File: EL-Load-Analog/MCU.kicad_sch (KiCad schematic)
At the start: 2 parts, among them J4 Conn_02x08_Odd_Even, J8 Conn_02x08_Odd_Even

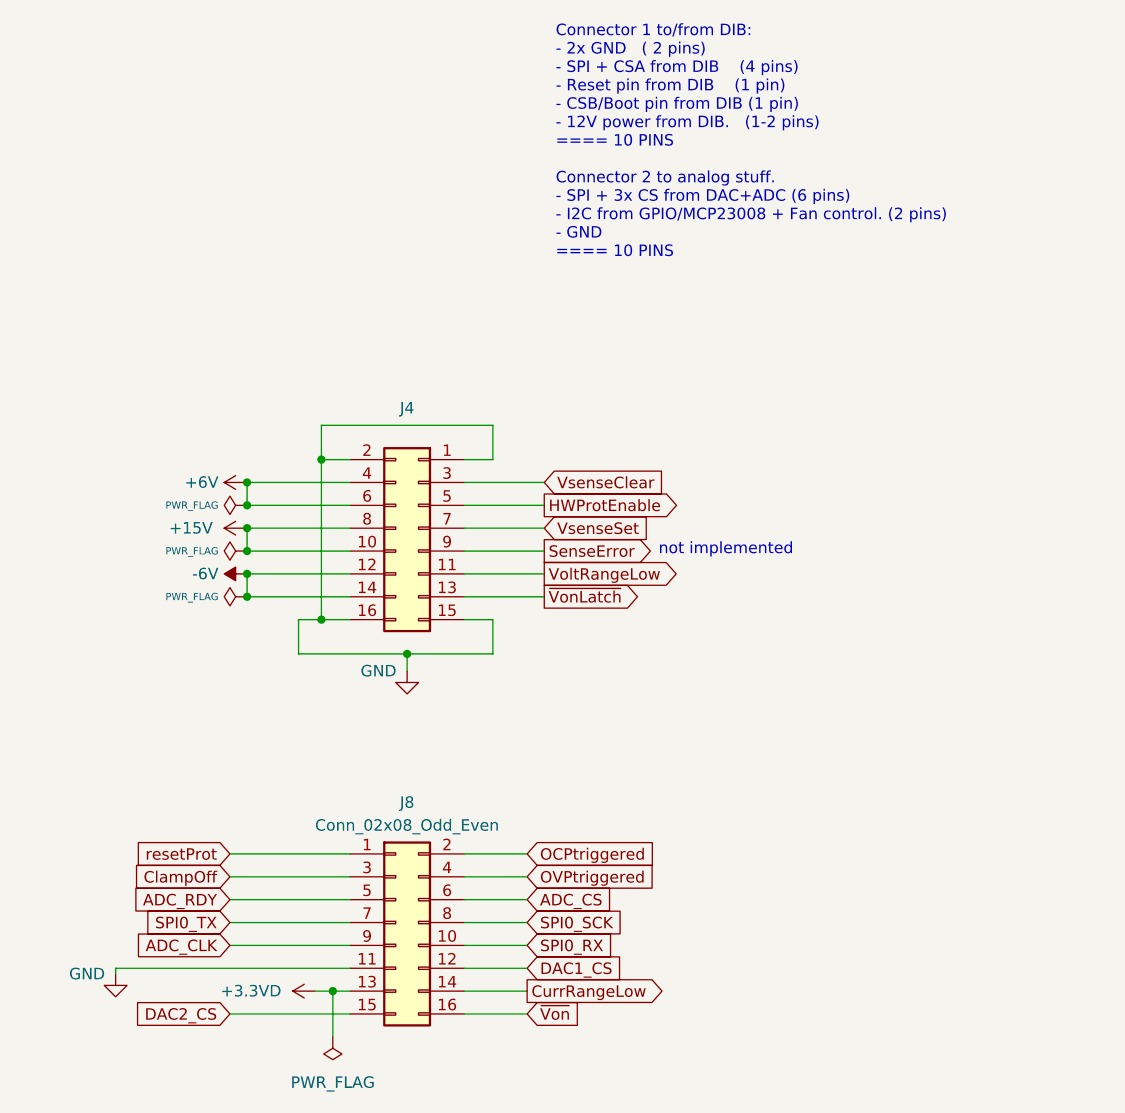
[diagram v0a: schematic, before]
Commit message: Added heatsink moutingholes, reverse polarity, moved snubbers.
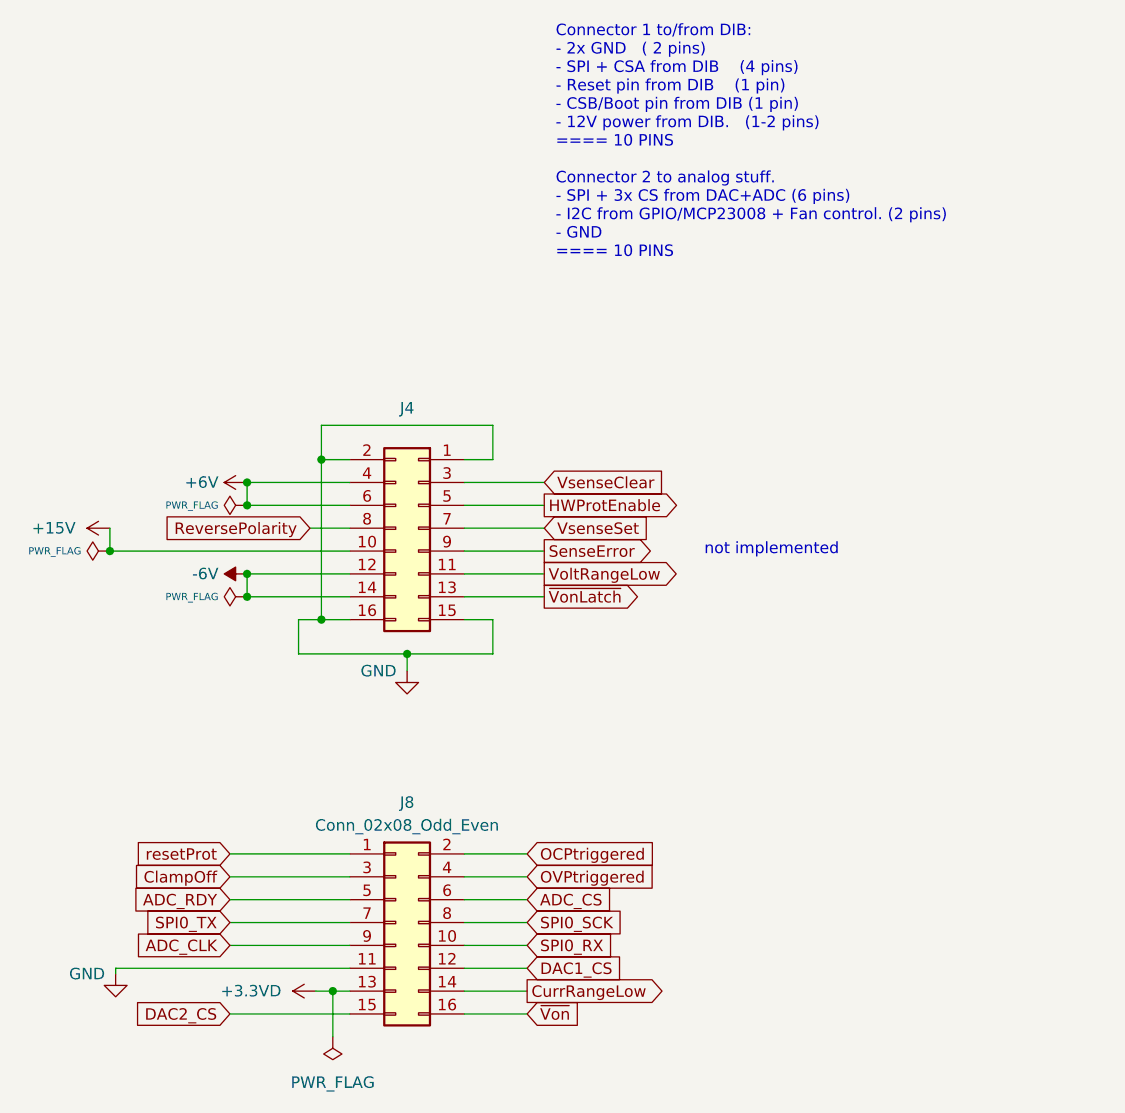
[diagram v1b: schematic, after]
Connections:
- net +15V: no longer J4.8 (Pin_8)
- new net ReversePolarity: J4.8 (Pin_8)
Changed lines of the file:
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@@
     (comment 1 "License: CERN-OHL-W-2.0")
   )
-  (junction (at 61.595 74.295) (diameter 0) (color 0 0 0 0)
-  )
-  (junction (at 61.595 71.755) (diameter 0) (color 0 0 0 0)
+  (junction (at 46.355 74.295) (diameter 0) (color 0 0 0 0)
   )
   (junction (at 69.85 81.915) (diameter 0) (color 0 0 0 0)
@@
     (stroke (width 0) (type default))
   )
-  (wire (pts (xy 61.595 71.755) (xy 61.595 74.295))
+  (wire (pts (xy 46.355 71.755) (xy 46.355 74.295))
     (stroke (width 0) (type default))
   )
@@
     (stroke (width 0) (type default))
   )
+  (wire (pts (xy 68.58 71.755) (xy 73.025 71.755))
+    (stroke (width 0) (type default))
+  )
   (wire (pts (xy 85.725 81.915) (xy 88.9 81.915))
     (stroke (width 0) (type default))
@@
     (stroke (width 0) (type default))
   )
-  (wire (pts (xy 61.595 74.295) (xy 73.025 74.295))
+  (wire (pts (xy 46.355 74.295) (xy 73.025 74.295))
     (stroke (width 0) (type default))
   )
@@
   )
   (wire (pts (xy 59.69 110.49) (xy 73.025 110.49))
-    (stroke (width 0) (type default))
-  )
-  (wire (pts (xy 61.595 71.755) (xy 73.025 71.755))
     (stroke (width 0) (type default))
   )
@@
     (effects (font (size 1.27 1.27)) (justify left bottom))
   )
-  (text "not implemented" (at 107.315 74.93 0)
+  (text "not implemented" (at 112.395 74.93 0)
     (effects (font (size 1.27 1.27)) (justify left bottom))
   )
@@
     (effects (font (size 1.27 1.27)) (justify left))
     (property "Intersheetrefs" "${INTERSHEET_REFS}" (at 99.0024 125.73 0)
-      (effects (font (size 1.27 1.27)) (justify left) hide)
+      (effects (font (size 1.27 1.27)) (justify left))
     )
   )
@@
     (effects (font (size 1.27 1.27)) (justify left))
     (property "Intersheetrefs" "${INTERSHEET_REFS}" (at 107.832 110.49 0)
-      (effects (font (size 1.27 1.27)) (justify left) hide)
+      (effects (font (size 1.27 1.27)) (justify left))
     )
   )
@@
     (effects (font (size 1.27 1.27)) (justify left))
     (property "Intersheetrefs" "${INTERSHEET_REFS}" (at 108.9204 123.19 0)
-      (effects (font (size 1.27 1.27)) (justify left) hide)
+      (effects (font (size 1.27 1.27)) (justify left))
     )
   )
@@
     (effects (font (size 1.27 1.27)) (justify left))
     (property "Intersheetrefs" "${INTERSHEET_REFS}" (at 103.901 120.65 0)
-      (effects (font (size 1.27 1.27)) (justify left) hide)
+      (effects (font (size 1.27 1.27)) (justify left))
     )
   )
@@
     (effects (font (size 1.27 1.27)) (justify left))
     (property "Intersheetrefs" "${INTERSHEET_REFS}" (at 102.1988 112.9506 0)
-      (effects (font (size 1.27 1.27)) (justify left) hide)
+      (effects (font (size 1.27 1.27)) (justify left))
     )
   )
@@
     (effects (font (size 1.27 1.27)) (justify left))
     (property "Intersheetrefs" "${INTERSHEET_REFS}" (at 107.095 71.755 0)
-      (effects (font (size 1.27 1.27)) (justify left) hide)
+      (effects (font (size 1.27 1.27)) (justify left))
     )
   )
@@
     (effects (font (size 1.27 1.27)) (justify left))
     (property "Intersheetrefs" "${INTERSHEET_REFS}" (at 106.0478 79.375 0)
-      (effects (font (size 1.27 1.27)) (justify left) hide)
+      (effects (font (size 1.27 1.27)) (justify left))
     )
   )
@@
     (effects (font (size 1.27 1.27)) (justify left))
     (property "Intersheetrefs" "${INTERSHEET_REFS}" (at 104.1341 115.4906 0)
-      (effects (font (size 1.27 1.27)) (justify left) hide)
+      (effects (font (size 1.27 1.27)) (justify left))
     )
   )
@@
     (effects (font (size 1.27 1.27)) (justify right))
     (property "Intersheetrefs" "${INTERSHEET_REFS}" (at 49.3457 115.57 0)
-      (effects (font (size 1.27 1.27)) (justify right) hide)
+      (effects (font (size 1.27 1.27)) (justify right))
     )
   )
@@
     (effects (font (size 1.27 1.27)) (justify left))
     (property "Intersheetrefs" "${INTERSHEET_REFS}" (at 108.0134 107.95 0)
-      (effects (font (size 1.27 1.27)) (justify left) hide)
+      (effects (font (size 1.27 1.27)) (justify left))
     )
   )
@@
     (effects (font (size 1.27 1.27)) (justify right))
     (property "Intersheetrefs" "${INTERSHEET_REFS}" (at 48.5594 113.03 0)
-      (effects (font (size 1.27 1.27)) (justify right) hide)
+      (effects (font (size 1.27 1.27)) (justify right))
     )
   )
@@
     (effects (font (size 1.27 1.27)) (justify left))
     (property "Intersheetrefs" "${INTERSHEET_REFS}" (at 107.7412 74.295 0)
-      (effects (font (size 1.27 1.27)) (justify left) hide)
+      (effects (font (size 1.27 1.27)) (justify left))
     )
   )
@@
     (effects (font (size 1.27 1.27)) (justify left))
     (property "Intersheetrefs" "${INTERSHEET_REFS}" (at 110.5834 69.215 0)
-      (effects (font (size 1.27 1.27)) (justify left) hide)
+      (effects (font (size 1.27 1.27)) (justify left))
     )
   )
@@
     (effects (font (size 1.27 1.27)) (justify right))
     (property "Intersheetrefs" "${INTERSHEET_REFS}" (at 48.1361 107.95 0)
-      (effects (font (size 1.27 1.27)) (justify right) hide)
+      (effects (font (size 1.27 1.27)) (justify right))
     )
   )
@@
     (effects (font (size 1.27 1.27)) (justify right))
     (property "Intersheetrefs" "${INTERSHEET_REFS}" (at 48.0758 110.49 0)
-      (effects (font (size 1.27 1.27)) (justify right) hide)
+      (effects (font (size 1.27 1.27)) (justify right))
     )
   )
@@
     (effects (font (size 1.27 1.27)) (justify left))
     (property "Intersheetrefs" "${INTERSHEET_REFS}" (at 109.0302 66.675 0)
-      (effects (font (size 1.27 1.27)) (justify left) hide)
+      (effects (font (size 1.27 1.27)) (justify left))
+    )
+  )
+  (global_label "ReversePolarity" (shape input) (at 68.58 71.755 180) (fields_autoplaced)
+    (effects (font (size 1.27 1.27)) (justify right))
+    (property "Intersheetrefs" "${INTERSHEET_REFS}" (at 50.9596 71.755 0)
+      (effects (font (size 1.27 1.27)) (justify right))
     )
   )
@@
     (effects (font (size 1.27 1.27)) (justify right))
     (property "Intersheetrefs" "${INTERSHEET_REFS}" (at 48.6199 118.11 0)
-      (effects (font (size 1.27 1.27)) (justify right) hide)
+      (effects (font (size 1.27 1.27)) (justify right))
     )
   )
@@
     (effects (font (size 1.27 1.27)) (justify left))
     (property "Intersheetrefs" "${INTERSHEET_REFS}" (at 110.4625 76.835 0)
-      (effects (font (size 1.27 1.27)) (justify left) hide)
+      (effects (font (size 1.27 1.27)) (justify left))
     )
   )
@@
     (effects (font (size 1.27 1.27)) (justify left))
     (property "Intersheetrefs" "${INTERSHEET_REFS}" (at 102.8641 118.0306 0)
-      (effects (font (size 1.27 1.27)) (justify left) hide)
+      (effects (font (size 1.27 1.27)) (justify left))
     )
   )
@@
     (effects (font (size 1.27 1.27)) (justify right))
     (property "Intersheetrefs" "${INTERSHEET_REFS}" (at 48.9917 125.6506 0)
-      (effects (font (size 1.27 1.27)) (justify right) hide)
+      (effects (font (size 1.27 1.27)) (justify right))
     )
   )
@@
     )
   )
-  (symbol (lib_id "power:+15V") (at 61.595 71.755 90) (unit 1)
-    (in_bom yes) (on_board yes) (dnp no) (fields_autoplaced)
-    (property "Reference" "#PWR0175" (at 65.405 71.755 0)
-      (effects (font (size 1.27 1.27)) hide)
-    )
-    (property "Value" "+15V" (at 57.785 71.755 90)
-      (effects (font (size 1.27 1.27)) (justify left))
-    )
-    (property "Footprint" "" (at 61.595 71.755 0)
-      (effects (font (size 1.27 1.27)) hide)
-    )
-    (property "Datasheet" "" (at 61.595 71.755 0)
+  (symbol (lib_id "power:+15V") (at 46.355 71.755 90) (unit 1)
+    (in_bom yes) (on_board yes) (dnp no) (fields_autoplaced)
+    (property "Reference" "#PWR0175" (at 50.165 71.755 0)
+      (effects (font (size 1.27 1.27)) hide)
+    )
+    (property "Value" "+15V" (at 42.545 71.755 90)
+      (effects (font (size 1.27 1.27)) (justify left))
+    )
+    (property "Footprint" "" (at 46.355 71.755 0)
+      (effects (font (size 1.27 1.27)) hide)
+    )
+    (property "Datasheet" "" (at 46.355 71.755 0)
       (effects (font (size 1.27 1.27)) hide)
     )
@@
     )
   )
-  (symbol (lib_id "power:PWR_FLAG") (at 61.595 74.295 90) (unit 1)
-    (in_bom yes) (on_board yes) (dnp no) (fields_autoplaced)
-    (property "Reference" "#FLG03" (at 59.69 74.295 0)
-      (effects (font (size 1.27 1.27)) hide)
-    )
-    (property "Value" "PWR_FLAG" (at 58.42 74.295 90)
+  (symbol (lib_id "power:PWR_FLAG") (at 46.355 74.295 90) (unit 1)
+    (in_bom yes) (on_board yes) (dnp no) (fields_autoplaced)
+    (property "Reference" "#FLG03" (at 44.45 74.295 0)
+      (effects (font (size 1.27 1.27)) hide)
+    )
+    (property "Value" "PWR_FLAG" (at 43.18 74.295 90)
       (effects (font (size 0.8 0.8)) (justify left))
     )
-    (property "Footprint" "" (at 61.595 74.295 0)
-      (effects (font (size 1.27 1.27)) hide)
-    )
-    (property "Datasheet" "~" (at 61.595 74.295 0)
-      (effects (font (size 1.27 1.27)) hide)
-    )
+    (property "Footprint" "" (at 46.355 74.295 0)
+      (effects (font (size 1.27 1.27)) hide)
+    )
+    (property "Datasheet" "~" (at 46.355 74.295 0)
+      (effects (font (size 1.27 1.27)) hide)
+    )

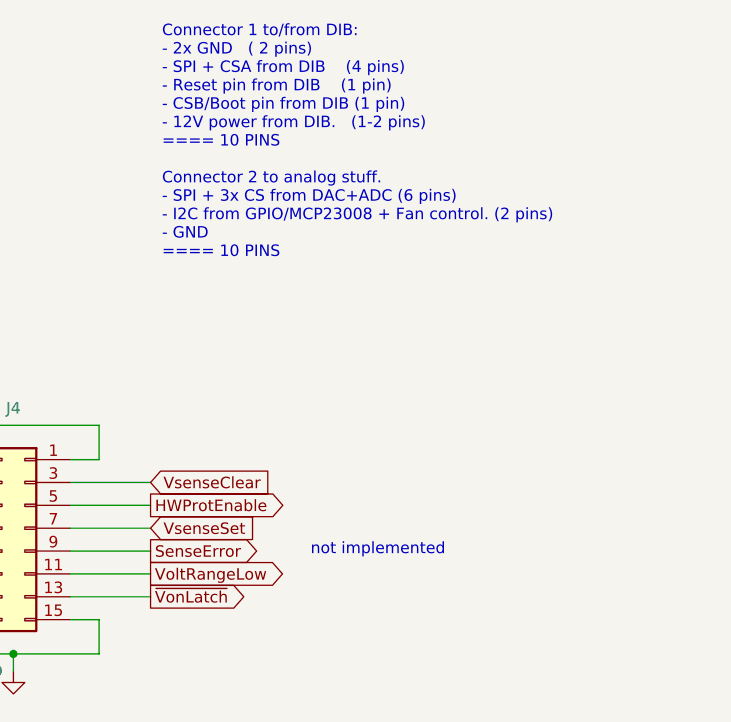
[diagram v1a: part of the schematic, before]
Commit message: v4 Analog board design. Features reverse polarity, remote sense error and new clamping circuitry.
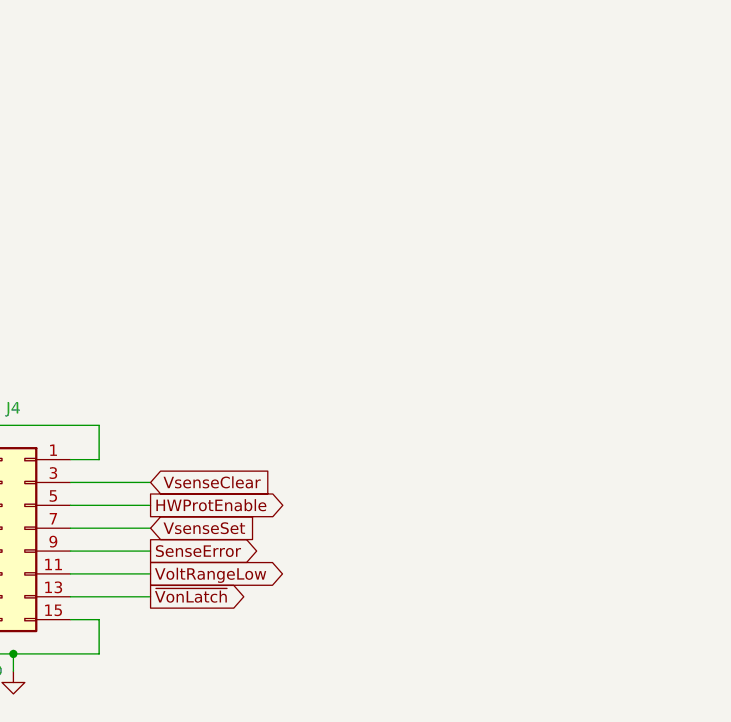
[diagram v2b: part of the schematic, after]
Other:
- note removed: "Connector 1 to/from DIB: - 2x GND ( 2 pins) - SPI + CSA from DIB (4 pins) - Reset pin from DIB (1 pin) - CSB/Boot pin from DIB (1 pin) - 12V power from DIB. (1-2 pins) ==== 10 PINS Connector 2 to analog stuff. - SPI + 3x CS from DAC+ADC (6 pins) - I2C from GPIO/MCP23008 + Fan control. (2 pins) - GND ==== 10 PINS"
- note removed: "not implemented"
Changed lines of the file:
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@@
   (title_block
     (title "Electronic Load Analog Test Board")
-    (date "2024-02-06")
+    (date "2024-11-10")
     (rev "${VERSION}")
     (comment 1 "License: CERN-OHL-W-2.0")
@@
     (stroke (width 0) (type default))
   )
-  (text "Connector 1 to/from DIB:\n- 2x GND   ( 2 pins)\n- SPI + CSA from DIB    (4 pins)\n- Reset pin from DIB    (1 pin)\n- CSB/Boot pin from DIB (1 pin)\n- 12V power from DIB.   (1-2 pins)\n==== 10 PINS\n\nConnector 2 to analog stuff.\n- SPI + 3x CS from DAC+ADC (6 pins)\n- I2C from GPIO/MCP23008 + Fan control. (2 pins)\n- GND\n==== 10 PINS\n"
-    (at 95.885 41.91 0)
-    (effects (font (size 1.27 1.27)) (justify left bottom))
-  )
-  (text "not implemented" (at 112.395 74.93 0)
-    (effects (font (size 1.27 1.27)) (justify left bottom))
-  )
   (global_label "~{Von}" (shape input) (at 92.71 125.73 0) (fields_autoplaced)
